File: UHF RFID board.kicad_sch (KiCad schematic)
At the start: 19 parts, among them J1 FZ_full_module, J10 SIM_Card, J2 picoblade, J4 Conn_02x05_Odd_Even, J5 Conn_02x04_Odd_Even, SW1 SW_SPDT, U1 YRM1001, U2 SEC1210

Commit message: changed the footprint for SIM card to the correct one
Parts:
- J10: footprint nard_sam:115c-bc00 sim simcard card connector -> Custom footprints:SIMMP-00801B000-G sim card connector
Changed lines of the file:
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@@
       (effects (font (size 1.27 1.27)) (justify left))
     )
-    (property "Footprint" "nard_sam:115c-bc00 sim simcard card connector" (at 262.89 45.72 0)
+    (property "Footprint" "Custom footprints:SIMMP-00801B000-G sim card connector" (at 262.89 45.72 0)
       (effects (font (size 1.27 1.27)) hide)
     )

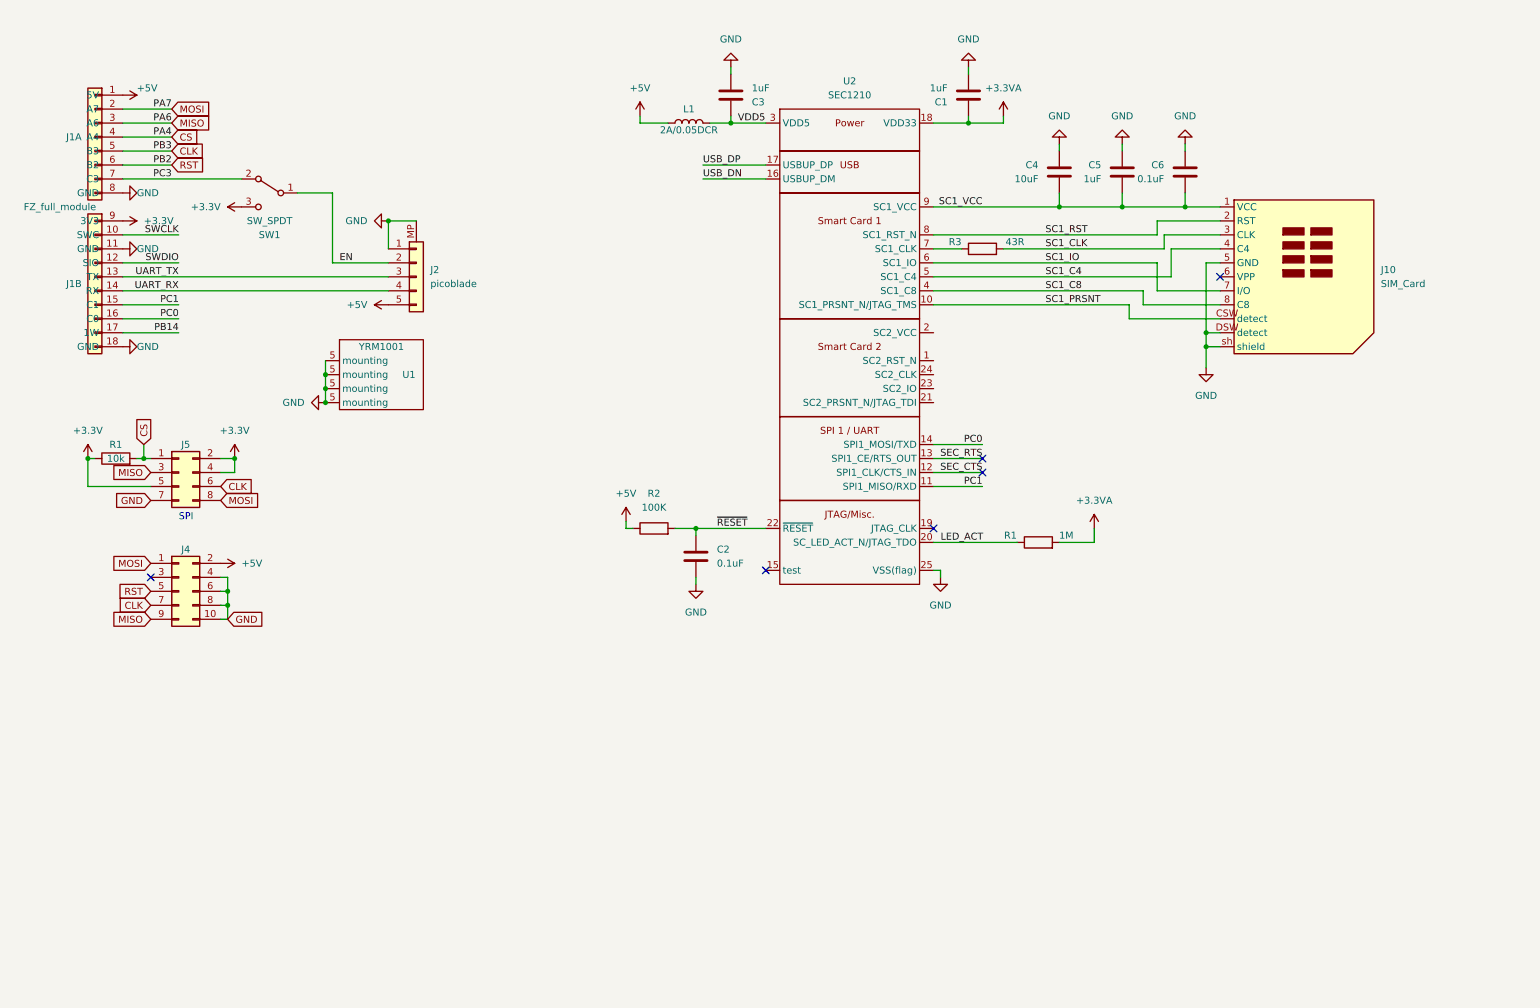
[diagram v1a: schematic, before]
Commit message: Add files via upload
updated board version to 1.2:
- changed ICSP from 10 pin header to 6 pin header. 10 pin ICSP connections can be done with a 6 to 10 pin adapter cable.
- changed name on board to UHF | RFID | SAM, removing '1/2 nard' from the name for clarity on what the board is and does.
- removed header that was meant to hard-connect the UHF module to the board: it is not used for communication with the board after all. 
- updated the QR codes designs for better machine readability
- various routing improvements.

schematics:
- changed ICSP from 10 pin header to 6 pin header

other:
reverse-engineered the YRM1001 and YRM200 boards to have them in Kicad. Measurements should be close enough for OKing designs using those modules.
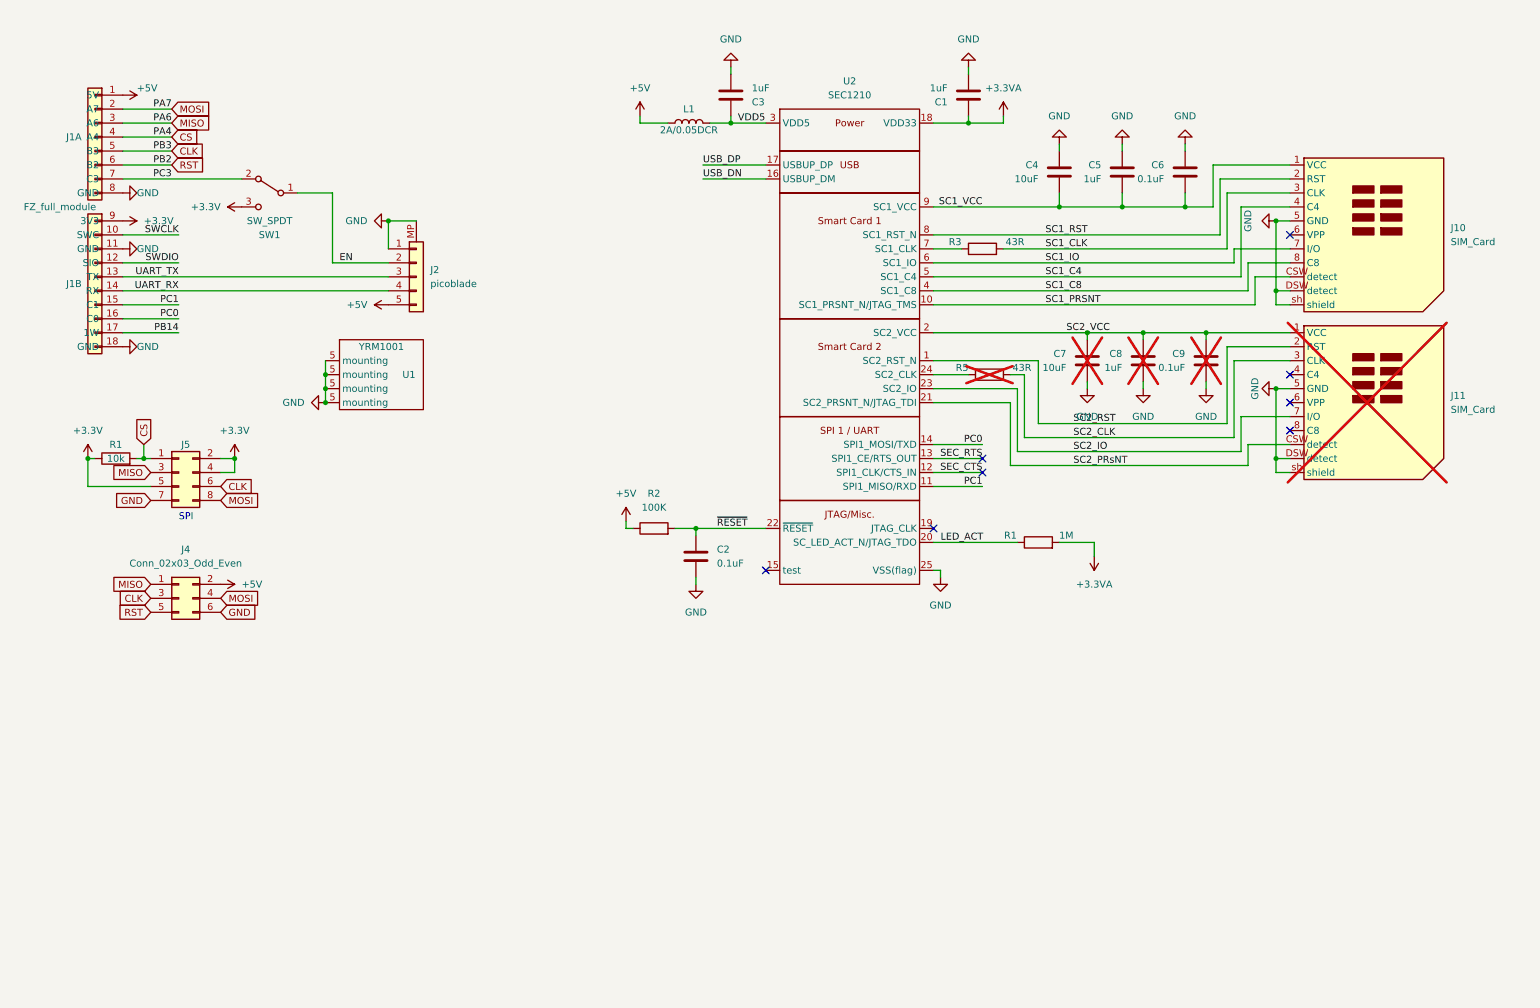
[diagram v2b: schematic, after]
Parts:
- removed J4: Conn_02x05_Odd_Even, Connector_PinHeader_2.54mm:PinHeader_2x05_P2.54mm_Vertical, symbol Connector_Generic:Conn_02x05_Odd_Even
- added C7: 10uF, Capacitor_SMD:C_0402_1005Metric, symbol Device:C
- added C8: 1uF, Capacitor_SMD:C_0402_1005Metric, symbol Device:C
- added C9: 0.1uF, Capacitor_SMD:C_0402_1005Metric, symbol Device:C
- added J11: SIM_Card, Custom footprints:SIMMP-00801B000-G sim card connector, symbol nard_sam:SIM_Card
- added J4: Conn_02x03_Odd_Even, Connector_PinHeader_2.54mm:PinHeader_2x03_P2.54mm_Vertical, symbol Connector_Generic:Conn_02x03_Odd_Even
- added R5: 43R, Resistor_SMD:R_0402_1005Metric, symbol Device:R
- U2: Datasheet local (none) -> N:\Flipper Zero\custom hardware\UHF RFID board\component da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
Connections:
- net +5V: now also J4.2 (Pin_2)
- net CLK: now also J4.3 (Pin_3)
- net GND: now also C7.1, C8.1, C9.1, J11.5 (GND), J11.DSW (detect), J11.sh (shield), J4.6 (Pin_6)
- net MISO: now also J4.1 (Pin_1)
- net MOSI: now also J4.4 (Pin_4)
- net RST: now also J4.5 (Pin_5)
- net SC2_RST: now reaches U2.1 (SC2_RST_N)
- net SC2_RST: now also J11.2 (RST)
- net SC2_VCC: now reaches U2.2 (SC2_VCC)
- net SC2_VCC: now also C7.2, C8.2, C9.2, J11.1 (VCC)
- net SC2_PRsNT: now reaches U2.21 (SC2_PRSNT_N/JTAG_TDI)
- net SC2_PRsNT: now also J11.CSW (detect)
- net SC2_IO: now reaches U2.23 (SC2_IO)
- net SC2_IO: now also J11.7 (I/O)
- net at U2.24 (SC2_CLK): now also R5.1
- new net SC2_CLK: J11.3 (CLK), R5.2
- no-connect marks 6 -> 8
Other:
- moved on the sheet: J10

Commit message: Version 2.0 RELEASE
- removed M3 support hole for 50x50 modules: there was only one M3 hole anyway, so no good mechanical support. case for the board can designed with mounting holes for that size module if need be.
- added second SAM slot as per SEC1210 datasheet.
- rerouted the vast majority of the board to accommodate all the changes.
- changed board thickness to 1.2 from 1.6 as per Flipper Zero module specs
- repositioned the SAM slots close to the board edge for ease of access to the SAMs with a case on.
- repositioned all of the components needed for the SEC1210 for addition of second SAM slot
- repositioned Picoblade connector for addition of second SAM slot
- repositioned ICSP and ISP headers for addition of second SAM slot
- updated legend to V2.0
- added GND and +5V vias near the usb connection for the SEC1210 in case they are needed.
- removed the selection switch and replaced it with a solder jumper. switch was overkill and this feature is there 'just in case': the YRM1001 does *NOT* have the enable pin actually routed on the module. It can be done but it requires desoldering the daughterboard from the module, cutting traces, and putting in bodge wires.
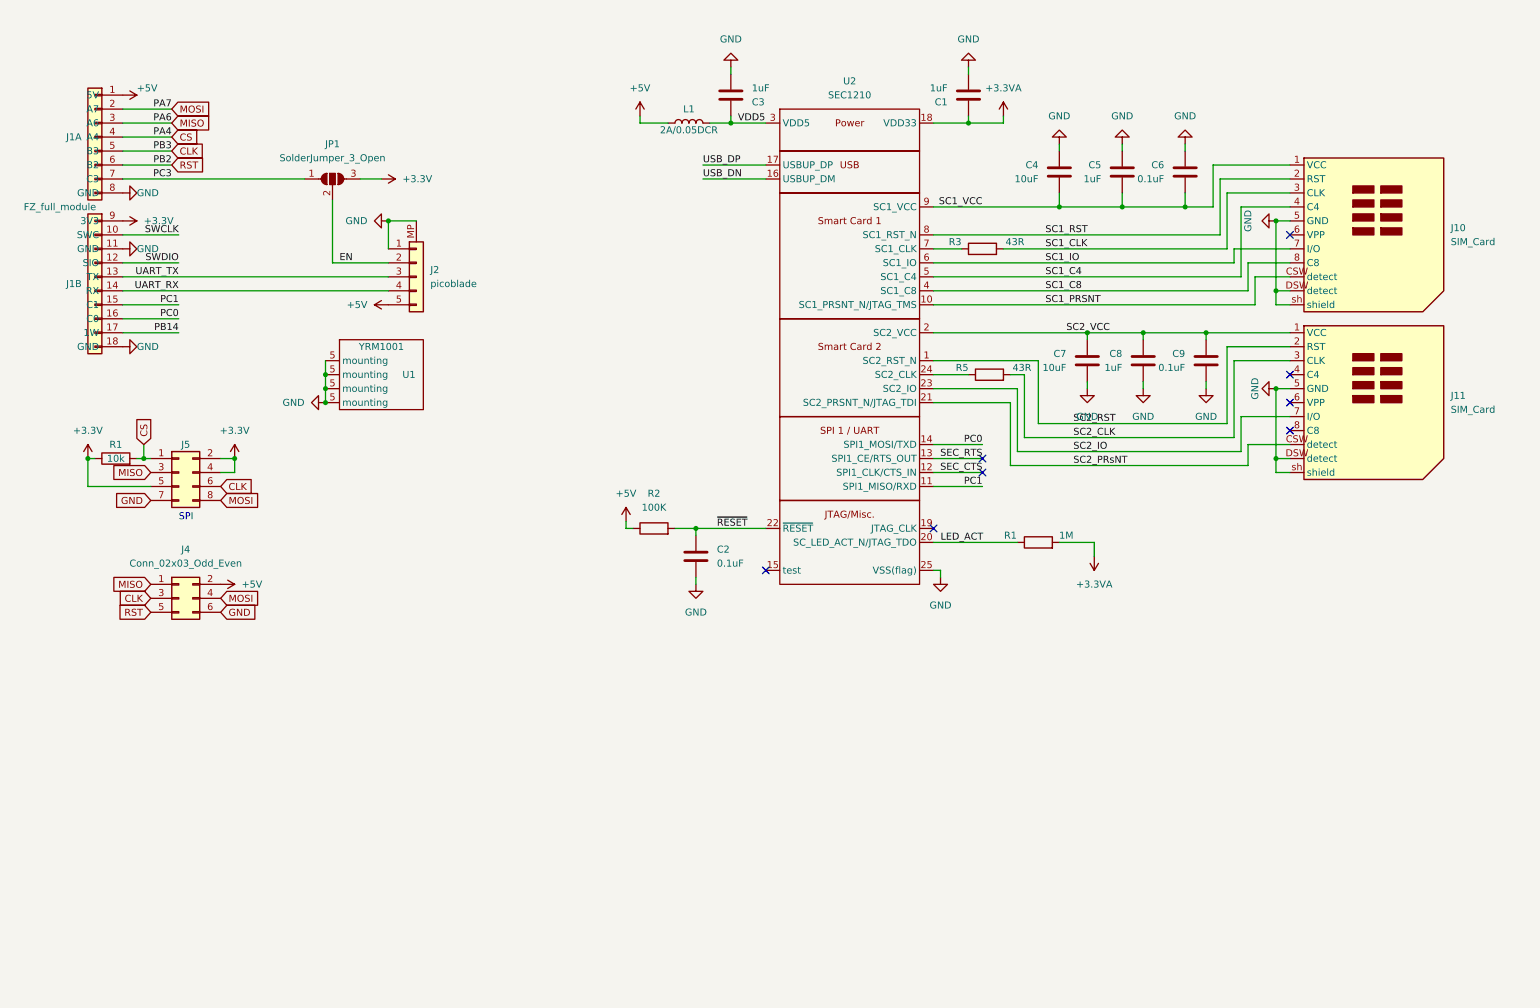
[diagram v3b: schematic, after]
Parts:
- removed SW1: SW_SPDT, Custom footprints:1K2 09.03201.02 SECME, symbol Switch:SW_SPDT
- added JP1: SolderJumper_3_Open, Jumper:SolderJumper-3_P2.0mm_Open_TrianglePad1.0x1.5mm, symbol Jumper:SolderJumper_3_Open
- C7, C8, C9, J11, R5: now fitted
- U1: footprint RFID_NFC_footprints:UHF_RFID_35x35_YRM1001_module_through-board no_header with mounting holes 35-40-50 -> RFID_NFC_footprints:UHF_RFID_35x35_YRM1001_module_through-board no_header with mounting holes 35-40
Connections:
- net +3.3V: now also JP1.3 (B)
- net EN: now also JP1.2 (C)
- net PC3: now also JP1.1 (A)
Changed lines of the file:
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@@
-    (stroke (width 0) (type default))
-  )
-  (wire (pts (xy 26.67 45.72) (xy 48.26 45.72))
     (stroke (width 0) (type default))
   )
@@
     (stroke (width 0) (type default))
   )
+  (wire (pts (xy 59.69 45.72) (xy 26.67 45.72))
+    (stroke (width 0) (type default))
+  )
   (wire (pts (xy 26.67 71.12) (xy 36.83 71.12))
     (stroke (width 0) (type default))
@@
     (stroke (width 0) (type default))
   )
+  (wire (pts (xy 69.85 45.72) (xy 73.66 45.72))
+    (stroke (width 0) (type default))
+  )
   (wire (pts (xy 44.45 99.06) (xy 46.99 99.06))
     (stroke (width 0) (type default))
@@
     (stroke (width 0) (type default))
   )
-  (wire (pts (xy 58.42 48.26) (xy 64.77 48.26))
+  (wire (pts (xy 64.77 49.53) (xy 64.77 60.96))
     (stroke (width 0) (type default))
   )
@@
   )
   (wire (pts (xy 224.79 43.18) (xy 238.76 43.18))
-    (stroke (width 0) (type default))
-  )
-  (wire (pts (xy 64.77 60.96) (xy 64.77 48.26))
     (stroke (width 0) (type default))
   )
@@
     )
   )
-  (symbol (lib_name "SW_SPDT_1") (lib_id "Switch:SW_SPDT") (at 53.34 48.26 0) (mirror y) (unit 1)
-    (in_bom yes) (on_board yes) (dnp no)
-    (property "Reference" "SW1" (at 53.34 55.88 0)
-      (effects (font (size 1.27 1.27)))
-    )
-    (property "Value" "SW_SPDT" (at 53.34 53.34 0)
-      (effects (font (size 1.27 1.27)))
-    )
-    (property "Footprint" "Custom footprints:1K2 09.03201.02 SECME" (at 54.61 43.18 0)
-      (effects (font (size 1.27 1.27)) hide)
-    )
-    (property "Datasheet" "~" (at 53.34 48.26 0)
-      (effects (font (size 1.27 1.27)) hide)
-    )
-    (property "mouser" "https://www.mouser.fr/ProductDetail/EAO/09.03201.02?qs=2pKMaj72wiEMFKWD2waFXQ%3D%3D" (at 53.34 48.26 0)
-      (effects (font (size 1.27 1.27)) hide)
-    )
-    (property "Aliexpress" "" (at 53.34 48.26 0)
-      (effects (font (size 1.27 1.27)) hide)
-    )
-    (pin "1")
-    (pin "2")
+  (symbol (lib_id "power:GND") (at 137.16 25.4 180) (unit 1)
+    (in_bom yes) (on_board yes) (dnp no) (fields_autoplaced)
+    (property "Reference" "#PWR021" (at 137.16 19.05 0)
+      (effects (font (size 1.27 1.27)) hide)
+    )
+    (property "Value" "GND" (at 137.16 20.32 0)
+      (effects (font (size 1.27 1.27)))
+    )
+    (property "Footprint" "" (at 137.16 25.4 0)
+      (effects (font (size 1.27 1.27)) hide)
+    )
+    (property "Datasheet" "" (at 137.16 25.4 0)
+      (effects (font (size 1.27 1.27)) hide)
+    )
+    (pin "1")
+    (instances
+      (project "UHF RFID board"
+        (path "/d8d0a45f-1f46-4ba4-9944-4b3c9d150d73"
+          (reference "#PWR021") (unit 1)
+        )
+      )
+    )
+  )
+  (symbol (lib_id "Jumper:SolderJumper_3_Open") (at 64.77 45.72 0) (unit 1)
+    (in_bom yes) (on_board yes) (dnp no) (fields_autoplaced)
+    (property "Reference" "JP1" (at 64.77 39.37 0)
+      (effects (font (size 1.27 1.27)))
+    )
+    (property "Value" "SolderJumper_3_Open" (at 64.77 41.91 0)
+      (effects (font (size 1.27 1.27)))
+    )
+    (property "Footprint" "Jumper:SolderJumper-3_P2.0mm_Open_TrianglePad1.0x1.5mm" (at 64.77 45.72 0)
+      (effects (font (size 1.27 1.27)) hide)
+    )
+    (property "Datasheet" "~" (at 64.77 45.72 0)
+      (effects (font (size 1.27 1.27)) hide)
+    )
+    (pin "2")
+    (pin "1")
     (pin "3")
     (instances
       (project "UHF RFID board"
         (path "/d8d0a45f-1f46-4ba4-9944-4b3c9d150d73"
-          (reference "SW1") (unit 1)
-        )
-      )
-    )
-  )
-  (symbol (lib_id "power:GND") (at 137.16 25.4 180) (unit 1)
-    (in_bom yes) (on_board yes) (dnp no) (fields_autoplaced)
-    (property "Reference" "#PWR021" (at 137.16 19.05 0)
-      (effects (font (size 1.27 1.27)) hide)
-    )
-    (property "Value" "GND" (at 137.16 20.32 0)
-      (effects (font (size 1.27 1.27)))
-    )
-    (property "Footprint" "" (at 137.16 25.4 0)
-      (effects (font (size 1.27 1.27)) hide)
-    )
-    (property "Datasheet" "" (at 137.16 25.4 0)
-      (effects (font (size 1.27 1.27)) hide)
-    )
-    (pin "1")
-    (instances
-      (project "UHF RFID board"
-        (path "/d8d0a45f-1f46-4ba4-9944-4b3c9d150d73"
-          (reference "#PWR021") (unit 1)
+          (reference "JP1") (unit 1)
         )
       )
@@
   )
   (symbol (lib_id "Device:C") (at 212.09 78.74 0) (mirror x) (unit 1)
-    (in_bom yes) (on_board no) (dnp yes) (fields_autoplaced)
+    (in_bom yes) (on_board yes) (dnp no) (fields_autoplaced)
     (property "Reference" "C8" (at 208.28 77.47 0)
       (effects (font (size 1.27 1.27)) (justify right))
@@
   )
   (symbol (lib_id "Device:C") (at 223.52 78.74 0) (mirror x) (unit 1)
-    (in_bom yes) (on_board no) (dnp yes) (fields_autoplaced)
+    (in_bom yes) (on_board yes) (dnp no) (fields_autoplaced)
     (property "Reference" "C9" (at 219.71 77.47 0)
       (effects (font (size 1.27 1.27)) (justify right))
@@
   )
   (symbol (lib_id "Device:C") (at 201.93 78.74 0) (mirror x) (unit 1)
-    (in_bom yes) (on_board no) (dnp yes) (fields_autoplaced)
+    (in_bom yes) (on_board yes) (dnp no) (fields_autoplaced)
     (property "Reference" "C7" (at 198.12 77.47 0)
       (effects (font (size 1.27 1.27)) (justify right))
@@
   )
   (symbol (lib_id "Device:R") (at 184.15 81.28 90) (unit 1)
-    (in_bom yes) (on_board no) (dnp yes)
+    (in_bom yes) (on_board yes) (dnp no)
     (property "Reference" "R5" (at 180.34 80.01 90)
       (effects (font (size 1.27 1.27)) (justify left))
@@
       (effects (font (size 1.27 1.27)))
     )
-    (property "Footprint" "RFID_NFC_footprints:UHF_RFID_35x35_YRM1001_module_through-board no_header with mounting holes 35-40-50" (at 66.04 76.2 0)
+    (property "Footprint" "RFID_NFC_footprints:UHF_RFID_35x35_YRM1001_module_through-board no_header with mounting holes 35-40" (at 66.04 76.2 0)
       (effects (font (size 1.27 1.27)) hide)
     )
@@
   )
   (symbol (lib_name "SIM_Card_1") (lib_id "nard_sam:SIM_Card") (at 251.46 81.28 0) (unit 1)
-    (in_bom yes) (on_board no) (dnp yes) (fields_autoplaced)
+    (in_bom yes) (on_board yes) (dnp no) (fields_autoplaced)
     (property "Reference" "J11" (at 267.97 85.09 0)
       (effects (font (size 1.27 1.27)) (justify left))
@@
     )
   )
-  (symbol (lib_id "power:+3.3V") (at 48.26 50.8 90) (unit 1)
-    (in_bom yes) (on_board yes) (dnp no) (fields_autoplaced)
-    (property "Reference" "#PWR011" (at 52.07 50.8 0)
-      (effects (font (size 1.27 1.27)) hide)
-    )
-    (property "Value" "+3.3V" (at 44.45 50.8 90)
+  (symbol (lib_id "power:+3.3V") (at 73.66 45.72 270) (unit 1)
+    (in_bom yes) (on_board yes) (dnp no) (fields_autoplaced)
+    (property "Reference" "#PWR011" (at 69.85 45.72 0)
+      (effects (font (size 1.27 1.27)) hide)
+    )
+    (property "Value" "+3.3V" (at 77.47 45.72 90)
       (effects (font (size 1.27 1.27)) (justify left))
     )
-    (property "Footprint" "" (at 48.26 50.8 0)
-      (effects (font (size 1.27 1.27)) hide)
-    )
-    (property "Datasheet" "" (at 48.26 50.8 0)
-      (effects (font (size 1.27 1.27)) hide)
-    )
+    (property "Footprint" "" (at 73.66 45.72 0)
+      (effects (font (size 1.27 1.27)) hide)
+    )
+    (property "Datasheet" "" (at 73.66 45.72 0)
+      (effects (font (size 1.27 1.27)) hide)
+    )
